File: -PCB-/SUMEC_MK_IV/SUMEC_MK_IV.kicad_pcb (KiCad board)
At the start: 2 copper layers, 82 parts, among them IC2 DRV8874PWPR, IC3 DRV8874PWPR, J2 TYPE-C-31-M-12, J3 Conn_01x06_Pin, J4 Conn_01x03_Pin, J5 Conn_01x06_Pin, J6 Conn_01x03_Pin, J7 Conn_01x06_Pin, J8 Conn_01x04_Pin, J9 Conn_01x03_Pin, SW1 SW_DPDT_x2, SW2 SW_Push, SW3 SW_Push, SW4 SW_Push, SW5 SW_Push, SW6 SW_Push, U1 TPS62133, U2 LM1084-3.3, U3 ESP32-S3-WROOM-1, U4 ESP32-S3-WROOM-1, U5 USBLC6-2SC6, U6 TSOP382xx

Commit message: Footprints added
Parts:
- removed C23, C24: 10uF.hb, Capacitor_Tantalum_SMD:CP_EIA-3216-18_Kemet-A_Pad1.58x1.35mm_HandSolder
- removed SW6: SW_Push, Button_Switch_SMD:SW_SPST_B3U-1000P
- removed U4: ESP32-S3-WROOM-1, PCM_Espressif:ESP32-S3-WROOM-1
- added C14: 100nF, Capacitor_SMD:C_0805_2012Metric_Pad1.18x1.45mm_HandSolder, F.Cu at (204.0, 91.0)
- added C17: 100nF.hb, Capacitor_SMD:C_0805_2012Metric_Pad1.18x1.45mm_HandSolder, F.Cu at (204.0, 100.1)
- added C18: 100nF.hb, Capacitor_SMD:C_0805_2012Metric_Pad1.18x1.45mm_HandSolder, F.Cu at (204.0, 103.1)
- added C19: 10uF.hb, Capacitor_Tantalum_SMD:CP_EIA-3216-18_Kemet-A_Pad1.58x1.35mm_HandSolder, F.Cu at (218.9, 101.7)
- added C20: 10uF.hb, Capacitor_Tantalum_SMD:CP_EIA-3216-18_Kemet-A_Pad1.58x1.35mm_HandSolder, F.Cu at (218.9, 104.8)
- added D1: D_Schottky, Diode_SMD:D_1206_3216Metric_Pad1.42x1.75mm_HandSolder, F.Cu at (170.0, 88.2)
- added D2: D_Schottky, Diode_SMD:D_1206_3216Metric_Pad1.42x1.75mm_HandSolder, F.Cu at (170.0, 91.6)
- added D6: LED, LED_SMD:LED_0805_2012Metric_Pad1.15x1.40mm_HandSolder, F.Cu at (102.7, 97.2)
- added D8: D_Schottky, Diode_SMD:D_1206_3216Metric_Pad1.42x1.75mm_HandSolder, F.Cu at (170.0, 95.0)
- added IC1: TPS565242DRLR, Package_TO_SOT_SMD:SOT-563, F.Cu at (184.5, 71.8)
- added J1: XT30PW-M, sumec_brd:XT30PW-M, F.Cu at (203.2, 69.8)
- added J10: Conn_01x04_Pin, Connector_Molex:Molex_PicoBlade_53398-0471_1x04-1MP_P1.25mm_Vertical, F.Cu at (125.3, 110.3)
- added J11: Conn_01x03_Pin, Connector_Molex:Molex_PicoBlade_53398-0371_1x03-1MP_P1.25mm_Vertical, F.Cu at (112.9, 124.2)
- added J12: TYPE-C-31-M-12, sumec-smdV2_library:USB_Type_C, F.Cu at (142.2, 40.5)
- added J13: Conn_01x06_Socket, Connector_JST:JST_SH_SM06B-SRSS-TB_1x06-1MP_P1.00mm_Horizontal, F.Cu at (126.8, 73.0)
- added J14: Conn_01x06_Socket, Connector_JST:JST_SH_SM06B-SRSS-TB_1x06-1MP_P1.00mm_Horizontal, F.Cu at (126.8, 80.6)
- added L1: 2.2uH, Inductor_SMD:L_Vishay_IHLP-1616, F.Cu at (172.8, 117.2)
- added L2: 1.5uH, Inductor_SMD:L_Vishay_IHLP-1212, F.Cu at (180.8, 71.8)
- added Q1: PMOS, Package_TO_SOT_SMD:SOT-23-3, F.Cu at (169.6, 99.1)
- added R20: 100R, Resistor_SMD:R_0805_2012Metric_Pad1.20x1.40mm_HandSolder, F.Cu at (102.6, 103.1)
- added R21: 100R, Resistor_SMD:R_0805_2012Metric_Pad1.20x1.40mm_HandSolder, F.Cu at (102.6, 106.1)
- added R22: 100R, Resistor_SMD:R_0805_2012Metric_Pad1.20x1.40mm_HandSolder, F.Cu at (102.6, 109.0)
- added R23: 0R, Resistor_SMD:R_0805_2012Metric_Pad1.20x1.40mm_HandSolder, F.Cu at (203.9, 119.9)
- added R24: 15R, Resistor_SMD:R_0805_2012Metric_Pad1.20x1.40mm_HandSolder, F.Cu at (203.9, 122.9)
- added R25: 15R, Resistor_SMD:R_0805_2012Metric_Pad1.20x1.40mm_HandSolder, F.Cu at (203.9, 125.8)
- added R5: 33k, Resistor_SMD:R_0805_2012Metric_Pad1.20x1.40mm_HandSolder, F.Cu at (138.7, 99.8)
- added R6: 10k, Resistor_SMD:R_0805_2012Metric_Pad1.20x1.40mm_HandSolder, F.Cu at (138.7, 102.8)
- C1: value 10uF.bck -> 22uF.vin; footprint Capacitor_Tantalum_SMD:CP_EIA-3216-18_Kemet-A_Pad1.58x1.35mm_HandSolder -> Capacitor_SMD:C_0805_2012Metric_Pad1.18x1.45mm_HandSolder
- C10: value 100nF -> 22uF; footprint Capacitor_SMD:C_0805_2012Metric -> Capacitor_Tantalum_SMD:CP_EIA-3528-21_Kemet-B_Pad1.50x2.35mm_HandSolder
- C11: value 10uF.reg -> 22uF; footprint Capacitor_Tantalum_SMD:CP_EIA-3216-18_Kemet-A_Pad1.58x1.35mm_HandSolder -> Capacitor_Tantalum_SMD:CP_EIA-3528-21_Kemet-B_Pad1.50x2.35mm_HandSolder
- C12: value 3.3nF -> 100nF.vout
- C13: value 10uF.reg -> 22nF; footprint Capacitor_Tantalum_SMD:CP_EIA-3216-18_Kemet-A_Pad1.58x1.35mm_HandSolder -> Capacitor_SMD:C_0805_2012Metric_Pad1.18x1.45mm_HandSolder
- C15: value 10uF.mcu -> 22nF; footprint Capacitor_Tantalum_SMD:CP_EIA-3216-18_Kemet-A_Pad1.58x1.35mm_HandSolder -> Capacitor_SMD:C_0805_2012Metric_Pad1.18x1.45mm_HandSolder
- C16: value 100nF.mcu -> 100nF
- C2: value 100nF.avin -> 100nF.vin
- C21, C22: value 100nF.hb -> 10uF.shrp; footprint Capacitor_SMD:C_0805_2012Metric_Pad1.18x1.45mm_HandSolder -> Capacitor_Tantalum_SMD:CP_EIA-3216-18_Kemet-A_Pad1.58x1.35mm_HandSolder
- C25: value 100nF.en -> 10uF.mcu; footprint Capacitor_SMD:C_0805_2012Metric_Pad1.18x1.45mm_HandSolder -> Capacitor_Tantalum_SMD:CP_EIA-3216-18_Kemet-A_Pad1.58x1.35mm_HandSolder
- C26: value 100nF.boot -> 100nF.mcu
- C28: value 10uF.shrp -> 100nF.en; footprint Capacitor_Tantalum_SMD:CP_EIA-3216-18_Kemet-A_Pad1.58x1.35mm_HandSolder -> Capacitor_SMD:C_0805_2012Metric_Pad1.18x1.45mm_HandSolder
- C29: value 10uF.shrp -> 100nF.boot; footprint Capacitor_Tantalum_SMD:CP_EIA-3216-18_Kemet-A_Pad1.58x1.35mm_HandSolder -> Capacitor_SMD:C_0805_2012Metric_Pad1.18x1.45mm_HandSolder
- C3: value 22uF -> 10uF.reg; footprint Capacitor_SMD:C_0805_2012Metric -> Capacitor_Tantalum_SMD:CP_EIA-3216-18_Kemet-A_Pad1.58x1.35mm_HandSolder
- C4: value 100nF -> 3.3nF; footprint Capacitor_SMD:C_0805_2012Metric -> Capacitor_SMD:C_0805_2012Metric_Pad1.18x1.45mm_HandSolder
- C5: value 10uF.mcu -> 10uF.pvin
- C6: value 100nF.mcu -> 10uF.reg; footprint Capacitor_SMD:C_0805_2012Metric_Pad1.18x1.45mm_HandSolder -> Capacitor_Tantalum_SMD:CP_EIA-3216-18_Kemet-A_Pad1.58x1.35mm_HandSolder
- C7: value 22uF -> 100nF.avin; footprint Capacitor_SMD:C_0805_2012Metric -> Capacitor_SMD:C_0805_2012Metric_Pad1.18x1.45mm_HandSolder
- C8, C9: footprint Capacitor_SMD:C_0805_2012Metric -> Capacitor_Tantalum_SMD:CP_EIA-3528-21_Kemet-B_Pad1.50x2.35mm_HandSolder
- D7: value LED -> D_Schottky; footprint LED_SMD:LED_0805_2012Metric_Pad1.15x1.40mm_HandSolder -> Diode_SMD:D_1206_3216Metric_Pad1.42x1.75mm_HandSolder
- J2: value TYPE-C-31-M-12 -> Conn_01x03_Pin; footprint sumec-smdV2_library:USB_Type_C -> Connector_Molex:Molex_PicoBlade_53398-0371_1x03-1MP_P1.25mm_Vertical
- J4, J6: value Conn_01x03_Pin -> Conn_01x06_Pin; footprint Connector_Molex:Molex_PicoBlade_53398-0371_1x03-1MP_P1.25mm_Vertical -> Connector_Molex:Molex_PicoBlade_53398-0671_1x06-1MP_P1.25mm_Vertical
- J5, J7: value Conn_01x06_Pin -> Conn_01x03_Pin; footprint Connector_Molex:Molex_PicoBlade_53398-0671_1x06-1MP_P1.25mm_Vertical -> Connector_Molex:Molex_PicoBlade_53398-0371_1x03-1MP_P1.25mm_Vertical
- J8: value Conn_01x04_Pin -> Conn_01x03_Pin; footprint Connector_Molex:Molex_PicoBlade_53398-0471_1x04-1MP_P1.25mm_Vertical -> Connector_Molex:Molex_PicoBlade_53398-0371_1x03-1MP_P1.25mm_Vertical
- R1: value 100k -> 20k; footprint Resistor_SMD:R_0805_2012Metric -> Resistor_SMD:R_0805_2012Metric_Pad1.20x1.40mm_HandSolder
- R10: value 10k.mcu -> 0R/R-Imode
- R11: value 0R -> 10k; footprint Resistor_SMD:R_1206_3216Metric_Pad1.30x1.75mm_HandSolder -> Resistor_SMD:R_0805_2012Metric_Pad1.20x1.40mm_HandSolder
- R12: value 15R -> 10k
- R13: value 15R -> 0R
- R14: value 10k -> 0R
- R15: value 100 -> 0R
- R16: value R -> 0R; footprint sumec-remote_library:purosidenegative -> Resistor_SMD:R_0805_2012Metric_Pad1.20x1.40mm_HandSolder
- R17: value R -> 10k; footprint sumec-smdV2_library:SPS LOGO -> Resistor_SMD:R_0805_2012Metric_Pad1.20x1.40mm_HandSolder
- R18: value R -> 100; footprint sumec-remote_library:boi -> Resistor_SMD:R_0805_2012Metric_Pad1.20x1.40mm_HandSolder
- R19: value R -> 560R; footprint sumec-smdV2_library:Logo -> Resistor_SMD:R_0805_2012Metric_Pad1.20x1.40mm_HandSolder
- R2: value 22k -> 30k; footprint Resistor_SMD:R_0805_2012Metric -> Resistor_SMD:R_0805_2012Metric_Pad1.20x1.40mm_HandSolder
- R26: value 0R -> 10k.mcu; footprint Resistor_SMD:R_1206_3216Metric_Pad1.30x1.75mm_HandSolder -> Resistor_SMD:R_0805_2012Metric_Pad1.20x1.40mm_HandSolder
- R27: value 0R -> R; footprint Resistor_SMD:R_1206_3216Metric_Pad1.30x1.75mm_HandSolder -> sumec-remote_library:purosidenegative
- R28: value 0R -> R; footprint Resistor_SMD:R_1206_3216Metric_Pad1.30x1.75mm_HandSolder -> sumec-smdV2_library:SPS LOGO
- R29: value 0R -> R; footprint Resistor_SMD:R_1206_3216Metric_Pad1.30x1.75mm_HandSolder -> sumec-remote_library:boi
- R3: value 150k -> 100k; footprint Resistor_SMD:R_0805_2012Metric -> Resistor_SMD:R_0805_2012Metric_Pad1.20x1.40mm_HandSolder
- R30: value 100R -> R; footprint Resistor_SMD:R_0805_2012Metric_Pad1.20x1.40mm_HandSolder -> sumec-smdV2_library:Logo
- R4: value 33k -> 150k; footprint Resistor_SMD:R_0805_2012Metric -> Resistor_SMD:R_0805_2012Metric_Pad1.20x1.40mm_HandSolder
- R7: value 100R -> 0R/R-Ipropi
- R8: value 100R -> 0R/R-Imode
- R9: value 560R -> 0R/R-Ipropi
- SW1: footprint sumec-smdV2_library:Custom_SPDT_4.8mm_Switch -> sumec_brd:Custom_SPDT_4.7mm_Switch
- SW2, SW3, SW4, SW5: footprint Button_Switch_SMD:SW_SPST_B3U-1000P -> Button_Switch_SMD:SW_SPST_EVQPE1
- TP1: footprint TestPoint:TestPoint_Loop_D1.80mm_Drill1.0mm_Beaded -> TestPoint:TestPoint_Pad_D1.0mm
- TP2: footprint TestPoint:TestPoint_Pad_D1.5mm -> TestPoint:TestPoint_Loop_D1.80mm_Drill1.0mm_Beaded
- TP4: footprint TestPoint:TestPoint_Pad_D1.5mm -> TestPoint:TestPoint_Pad_1.0x1.0mm
- U1: value TPS62133 -> LM1084-3.3; footprint Package_DFN_QFN:VQFN-16-1EP_3x3mm_P0.5mm_EP1.68x1.68mm_ThermalVias -> Package_TO_SOT_SMD:TO-263-3_TabPin2
- U2: value LM1084-3.3 -> TPS62133; footprint Package_TO_SOT_SMD:TO-263-3_TabPin2 -> Package_DFN_QFN:VQFN-16-1EP_3x3mm_P0.5mm_EP1.68x1.68mm_ThermalVias
- U3: value ESP32-S3-WROOM-1 -> TSOP382xx; footprint RF_Module:ESP32-S3-WROOM-1 -> sumec-smdV2_library:TSOP
- U5: value USBLC6-2SC6 -> ESP32-S3-WROOM-1; footprint Package_TO_SOT_SMD:TSOT-23-6_HandSoldering -> RF_Module:ESP32-S3-WROOM-1
- U6: value TSOP382xx -> USBLC6-2SC6; footprint sumec-smdV2_library:TSOP -> Package_TO_SOT_SMD:TSOT-23-6_HandSoldering
- moved R16 151.2 mm to (213.5, 96.8)
- moved TP5 141.9 mm to (259.5, 67.2)
- moved TP6 141.4 mm to (259.5, 72.1)
- moved R27 138.5 mm to (74.6, 58.5)
- moved TP1 136.9 mm to (245.2, 61.8)
- moved U5 135.4 mm to (75.7, 114.8)
- moved R28 135.0 mm to (201.9, -20.3)
- moved R17 130.3 mm to (131.8, 115.8)
- moved TP4 126.8 mm to (242.2, 61.8)
- moved H1 125.2 mm to (240.8, 102.5)
- moved H2 125.2 mm to (240.8, 110.5)
- moved H3 125.2 mm to (240.8, 118.4)
- moved H4 125.2 mm to (240.8, 126.3)
- moved TP3 122.3 mm to (239.0, 61.8)
- moved R8 122.2 mm to (208.8, 91.0)
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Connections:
- C1 pad 1: +12V -> Net-(IC1-VIN)
- C1 pad 2: GND -> +5V
- C10 pad 1: VCC -> +3V3
- C11 pad 1: +5V -> +3V3
- C12 pad 1: GND -> +3V3
- C12 pad 2: Net-(U1-SS/TR) -> GND
- C13 pad 1: +3V3 -> Net-(IC2-CPL)
- C13 pad 2: GND -> Net-(IC2-CPH)
- C15 pad 1: +3V3 -> Net-(IC3-CPL)
- C15 pad 2: GND -> Net-(IC3-CPH)
- C16 pad 1: +3V3 -> Net-(IC3-VCP)
- C16 pad 2: GND -> +12V
- C2 pad 1: +12V -> Net-(IC1-VIN)
- C2 pad 2: GND -> +5V
- C21 pad 1: GND -> +3V3
- C21 pad 2: +12V -> GND
- C22 pad 1: GND -> +3V3
- C22 pad 2: +12V -> GND
- C25 pad 1: EN -> +3V3
- C26 pad 1: BOOT -> +3V3
- C28 pad 1: +3V3 -> EN
- C29 pad 1: +3V3 -> BOOT
- C4 pad 1: +5V -> GND
- C4 pad 2: GND -> Net-(U2-SS/TR)
- C5 pad 1: +3V3 -> +12V
- C7 pad 1: VCC -> +12V
- C8 pad 1: VCC -> VOUT 5V
- C9 pad 1: VCC -> +3V3
- D3 pad 2: LED1 -> +12V
- D5 pad 2: +12V -> LED2
- D7 pad 1: Net-(D7-K) -> VBUS 5V
- D7 pad 2: LED2 -> Net-(D7-A)
- J4 pad 1: SHARP 1 -> +5V
- J4 pad 2: +3V3 -> SDA
- J4 pad 3: GND -> SCL
- J5 pad 1: +5V -> SHARP 2
- J5 pad 2: SDA -> +3V3
- J5 pad 3: SCL -> GND
- J6 pad 1: SHARP 2 -> +5V
- J6 pad 2: +3V3 -> SDA
- J6 pad 3: GND -> SCL
- J7 pad 1: +5V -> POL 3
- J7 pad 2: SDA -> +3V3
- J7 pad 3: SCL -> GND
- J8 pad 1: QRE1113 A -> POL 1
- J8 pad 2: GND -> +3V3
- J8 pad 3: +3V3 -> GND
- J9 pad 1: QRE1113 C -> POL 2
- J9 pad 2: Net-(J9-Pin_2) -> +3V3
- R1 pad 1: +5V -> Net-(D8-K)
- R1 pad 2: /POWER_SUPPLY/En_3V3 -> +5V
- R10 pad 1: EN -> GND
- R10 pad 2: +3V3 -> Net-(IC3-IMODE)
- R11 pad 1: Net-(J2-SHIELD-PadS1) -> +3V3
- R11 pad 2: GND -> nFAULT
- R12 pad 1: D+ IN -> +3V3
- R12 pad 2: Net-(R12-Pad2) -> nFAULT
- R13 pad 1: D- IN -> GND
- R13 pad 2: Net-(R13-Pad2) -> Net-(IC2-PMODE)
- R14 pad 2: QRE1113 C -> Net-(IC2-PMODE)
- R15 pad 1: +3V3 -> GND
- R15 pad 2: Net-(J9-Pin_2) -> Net-(IC3-PMODE)
- R2 pad 1: /POWER_SUPPLY/En_3V3 -> Net-(D8-K)
- R26 pad 1: GND -> EN
- R26 pad 2: Net-(IC2-PMODE) -> +3V3
- R3 pad 1: VCC -> VOUT 5V
- R3 pad 2: Net-(IC1-FB) -> Net-(U2-PG)
- R4 pad 1: Net-(IC1-FB) -> +3V3
- R4 pad 2: GND -> FB
- R7 pad 1: Net-(D3-K) -> GND
- R7 pad 2: GND -> IPROPI_ADC
- R8 pad 1: Net-(D4-K) -> GND
- R8 pad 2: GND -> Net-(IC2-IMODE)
- R9 pad 1: Net-(D5-K) -> GND
- R9 pad 2: GND -> IPROPI_ADC
- SW4 pad 2: TEST PROGRAM -> TEST PROGRAM 1
- SW5 pad 2: unconnected-(SW5-Pad2) -> TEST PROGRAM 2
- TP1 pad 1: +3V3 -> +5V
- TP2 pad 1: SCL -> +3V3
- TP3 pad 1: SDA -> unconnected-(TP3-Pad1)
- TP4 pad 1: D- -> unconnected-(TP4-Pad1)
- TP5 pad 1: +5V -> D-
- U1 pad 1: Net-(L2-Pad1) -> GND
- U1 pad 2: Net-(L2-Pad1) -> +3V3
- U1 pad 3: Net-(L2-Pad1) -> +5V
- U2 pad 1: GND -> Net-(L1-Pad1)
- U2 pad 2: +3V3 -> Net-(L1-Pad1)
- U2 pad 3: +5V -> Net-(L1-Pad1)
- U3 pad 1: Net-(U3-GND-Pad1) -> IR MODULE
- U3 pad 2: +3V3 -> GND
- U3 pad 3: EN -> +3V3
- U5 pad 1: Net-(R12-Pad2) -> Net-(U5-GND-Pad1)
- U5 pad 2: GND -> +3V3
- U5 pad 3: Net-(R13-Pad2) -> EN
- U5 pad 4: D- -> QRE1113 B
- U5 pad 5: VBUS 5V -> QRE1113 A
- U5 pad 6: D+ -> QRE1113 C
- U6 pad 1: IR MODULE -> Net-(R24-Pad2)
- U6 pad 3: +3V3 -> Net-(R25-Pad2)

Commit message: MK_IV PCB update
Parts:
- removed C28: 100nF.en, Capacitor_SMD:C_0805_2012Metric_Pad1.18x1.45mm_HandSolder
- removed C29: 100nF.boot, Capacitor_SMD:C_0805_2012Metric_Pad1.18x1.45mm_HandSolder
- removed U6: USBLC6-2SC6, Package_TO_SOT_SMD:TSOT-23-6_HandSoldering
- added C23: 10uF.mcu, Capacitor_Tantalum_SMD:CP_EIA-3216-18_Kemet-A_Pad1.58x1.35mm_HandSolder, B.Cu at (183.5, 118.0)
- added C24: 100nF.mcu, Capacitor_SMD:C_0805_2012Metric_Pad1.18x1.45mm_HandSolder, B.Cu at (181.2, 117.5)
- added U4: ESP32-S3-WROOM-1, RF_Module:ESP32-S3-WROOM-1, F.Cu at (190.0, 120.5)
- C1: value 22uF.vin -> 10uF.reg; footprint Capacitor_SMD:C_0805_2012Metric_Pad1.18x1.45mm_HandSolder -> Capacitor_Tantalum_SMD:CP_EIA-3216-18_Kemet-A_Pad1.58x1.35mm_HandSolder
- C10, C11, C12, C5, C9, D1, D2, IC1, Q1, R23, R26, R4, R5, U2: moved to B.Cu
- C2: value 100nF.vin -> 10uF.reg; footprint Capacitor_SMD:C_0805_2012Metric_Pad1.18x1.45mm_HandSolder -> Capacitor_Tantalum_SMD:CP_EIA-3216-18_Kemet-A_Pad1.58x1.35mm_HandSolder
- C25: value 10uF.mcu -> 100nF; footprint Capacitor_Tantalum_SMD:CP_EIA-3216-18_Kemet-A_Pad1.58x1.35mm_HandSolder -> Capacitor_SMD:C_0805_2012Metric_Pad1.18x1.45mm_HandSolder
- C26: value 100nF.mcu -> 100nF.en; moved to B.Cu
- C27: value 100nF -> 100nF.boot; moved to B.Cu
- C3: value 10uF.reg -> 3.3nF; footprint Capacitor_Tantalum_SMD:CP_EIA-3216-18_Kemet-A_Pad1.58x1.35mm_HandSolder -> Capacitor_SMD:C_0805_2012Metric_Pad1.18x1.45mm_HandSolder; moved to B.Cu
- C4: value 3.3nF -> 22uF; footprint Capacitor_SMD:C_0805_2012Metric_Pad1.18x1.45mm_HandSolder -> Capacitor_Tantalum_SMD:CP_EIA-3528-21_Kemet-B_Pad1.50x2.35mm_HandSolder; moved to B.Cu
- C6: value 10uF.reg -> 100nF.vin; footprint Capacitor_Tantalum_SMD:CP_EIA-3216-18_Kemet-A_Pad1.58x1.35mm_HandSolder -> Capacitor_SMD:C_0805_2012Metric_Pad1.18x1.45mm_HandSolder; moved to B.Cu
- C7: value 100nF.avin -> 22uF; footprint Capacitor_SMD:C_0805_2012Metric_Pad1.18x1.45mm_HandSolder -> Capacitor_Tantalum_SMD:CP_EIA-3528-21_Kemet-B_Pad1.50x2.35mm_HandSolder; moved to B.Cu
- C8: value 22uF -> 100nF.avin; footprint Capacitor_Tantalum_SMD:CP_EIA-3528-21_Kemet-B_Pad1.50x2.35mm_HandSolder -> Capacitor_SMD:C_0805_2012Metric_Pad1.18x1.45mm_HandSolder; moved to B.Cu
- D3: value LED -> D_Schottky; footprint LED_SMD:LED_0805_2012Metric_Pad1.15x1.40mm_HandSolder -> Diode_SMD:D_1206_3216Metric_Pad1.42x1.75mm_HandSolder; moved to B.Cu
- D7: value D_Schottky -> LED; footprint Diode_SMD:D_1206_3216Metric_Pad1.42x1.75mm_HandSolder -> LED_SMD:LED_0805_2012Metric_Pad1.15x1.40mm_HandSolder
- L1: value 2.2uH -> 1.5uH; footprint Inductor_SMD:L_Vishay_IHLP-1616 -> Inductor_SMD:L_Vishay_IHLP-1212; moved to B.Cu
- L2: value 1.5uH -> 2.2uH; footprint Inductor_SMD:L_Vishay_IHLP-1212 -> Inductor_SMD:L_Vishay_IHLP-1616; moved to B.Cu
- R1: value 20k -> 10k; moved to B.Cu
- R2: value 30k -> 20k; moved to B.Cu
- R3: value 100k -> 30k; moved to B.Cu
- R6: value 10k -> 100k; moved to B.Cu
- TP3: footprint TestPoint:TestPoint_Pad_D1.5mm -> TestPoint:TestPoint_Pad_1.0x1.0mm
- TP4: footprint TestPoint:TestPoint_Pad_1.0x1.0mm -> TestPoint:TestPoint_Pad_D1.5mm
- U5: value ESP32-S3-WROOM-1 -> USBLC6-2SC6; footprint RF_Module:ESP32-S3-WROOM-1 -> Package_TO_SOT_SMD:TSOT-23-6_HandSoldering
- moved R27 156.4 mm to (-68.2, -5.34)
- moved R28 156.4 mm to (59.1, -84.1)
- moved R29 156.4 mm to (-35.5, -10.2)
- moved R30 156.4 mm to (-23.6, -25.9)
- moved TP5 153.4 mm to (154.2, 178.8)
- moved TP6 152.4 mm to (154.2, 182.3)
- moved C26 146.2 mm to (205.2, 116.8)
- moved TP4 143.6 mm to (154.2, 175.2)
- moved TP1 143.2 mm to (157.5, 174.9)
- moved TP3 142.0 mm to (157.5, 178.0)
- moved TP2 133.3 mm to (166.2, 175.8)
- moved C2 129.0 mm to (278.0, 29.5), turned to 90 degrees
- moved C1 125.3 mm to (275.5, 29.5), turned to 90 degrees
- moved U1 120.1 mm to (278.0, 42.4), turned to -90 degrees
- moved D4 113.8 mm to (206.2, 138.2), turned to 90 degrees
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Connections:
- C1 pad 1: Net-(IC1-VIN) -> +5V
- C1 pad 2: +5V -> GND
- C10 pad 2: GND -> Net-(C10-Pad2)
- C11 pad 1: +3V3 -> VOUT 5V
- C12 pad 2: GND -> Net-(C10-Pad2)
- C2 pad 1: Net-(IC1-VIN) -> +3V3
- C2 pad 2: +5V -> GND
- C25 pad 1: +3V3 -> VBUS 5V
- C26 pad 1: +3V3 -> EN
- C27 pad 1: VBUS 5V -> BOOT
- C3 pad 1: +5V -> GND
- C3 pad 2: GND -> Net-(U2-SS/TR)
- C4 pad 1: GND -> +5V
- C4 pad 2: Net-(U2-SS/TR) -> GND
- C6 pad 1: +3V3 -> +5V
- C7 pad 1: +12V -> +3V3
- C7 pad 2: GND -> Net-(C10-Pad2)
- C8 pad 1: VOUT 5V -> +12V
- C9 pad 2: GND -> Net-(C10-Pad2)
- D3 pad 2: +12V -> GND
- D4 pad 2: LED2 -> +12V
- D5 pad 2: LED2 -> LED1
- D6 pad 2: LED1 -> LED2
- D7 pad 1: VBUS 5V -> Net-(D7-K)
- D7 pad 2: Net-(D7-A) -> LED3
- D8 pad 1: Net-(D8-K) -> VBUS 5V
- D8 pad 2: GND -> Net-(D8-A)
- IC1 pad 1: Net-(IC1-VIN) -> +5V
- IC1 pad 5: Net-(D8-K) -> Net-(D3-K)
- J12 pad A4_B9: Net-(D7-A) -> Net-(D8-A)
- J12 pad B4_A9: Net-(D7-A) -> Net-(D8-A)
- L1 pad 1: Net-(L1-Pad1) -> Net-(IC1-SW)
- L1 pad 2: VOUT 5V -> +3V3
- L2 pad 1: Net-(IC1-SW) -> Net-(L2-Pad1)
- L2 pad 2: +3V3 -> VOUT 5V
- R1 pad 1: Net-(D8-K) -> VBUS 5V
- R1 pad 2: +5V -> GND
- R19 pad 1: Net-(D3-K) -> Net-(D4-K)
- R2 pad 1: Net-(D8-K) -> Net-(D3-K)
- R2 pad 2: GND -> +5V
- R20 pad 1: Net-(D4-K) -> Net-(D5-K)
- R21 pad 1: Net-(D5-K) -> Net-(D6-K)
- R22 pad 1: Net-(D6-K) -> Net-(D7-K)
- R3 pad 1: VOUT 5V -> Net-(D3-K)
- R3 pad 2: Net-(U2-PG) -> GND
- R6 pad 1: VBUS 5V -> VOUT 5V
- R6 pad 2: GND -> Net-(U2-PG)
- U2 pad 1: Net-(L1-Pad1) -> Net-(L2-Pad1)
- U2 pad 2: Net-(L1-Pad1) -> Net-(L2-Pad1)
- U2 pad 3: Net-(L1-Pad1) -> Net-(L2-Pad1)
- U5 pad 1: Net-(U5-GND-Pad1) -> Net-(R24-Pad2)
- U5 pad 2: +3V3 -> GND
- U5 pad 3: EN -> Net-(R25-Pad2)
- U5 pad 4: QRE1113 B -> D-
- U5 pad 5: QRE1113 A -> VBUS 5V
- U5 pad 6: QRE1113 C -> D+
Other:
- board outline added: 80 x 45 mm
- copper layers 2 -> 4

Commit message: MK_IV layout update
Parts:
- removed TP6: TestPoint, TestPoint:TestPoint_Pad_D1.5mm
- C14, C16, C19, C20, C21, C22, J10, J11, J13, J14, J2, J5, J7, J8, J9, R11, R12, R14, R16, R17, R18: moved to B.Cu
- TP1: footprint TestPoint:TestPoint_Pad_D1.0mm -> TestPoint:TestPoint_Pad_1.0x1.0mm
- TP2: footprint TestPoint:TestPoint_Loop_D1.80mm_Drill1.0mm_Beaded -> TestPoint:TestPoint_Pad_1.0x1.0mm
- TP4, TP5: footprint TestPoint:TestPoint_Pad_D1.5mm -> TestPoint:TestPoint_Pad_1.0x1.0mm
- moved J2 118.5 mm to (219.4, 136.2), turned to -90 degrees
- moved J7 111.9 mm to (213.0, 154.7), turned to 180 degrees
- moved J11 106.6 mm to (190.0, 117.3)
- moved J9 101.7 mm to (201.8, 154.7), turned to 180 degrees
- moved C19 100.8 mm to (188.0, 143.2), turned to 90 degrees
- moved IC2 100.1 mm to (193.0, 146.2), turned to 180 degrees
- moved J3 97.4 mm to (211.0, 155.8), turned to 180 degrees
- moved IC3 97.0 mm to (207.8, 146.2), turned to 180 degrees
- moved C20 95.5 mm to (202.8, 143.2), turned to 90 degrees
- moved R13 95.3 mm to (191.0, 150.0), turned to 180 degrees
- moved R15 94.2 mm to (205.8, 150.0), turned to 180 degrees
- moved R14 93.6 mm to (191.0, 150.0), turned to 180 degrees
- moved R16 91.9 mm to (205.8, 150.0), turned to 180 degrees
- moved J13 90.2 mm to (195.1, 134.1)
- moved C13 88.8 mm to (188.0, 147.8), turned to 90 degrees
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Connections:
- TP3 pad 1: unconnected-(TP3-Pad1) -> IR MODULE
- TP4 pad 1: unconnected-(TP4-Pad1) -> OUT 1A
- TP5 pad 1: D- -> OUT 1B

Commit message: PCB routing
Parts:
- U3: footprint sumec-smdV2_library:TSOP -> sumec_brd:TSOP
- moved J14 2.43 mm to (183.5, 132.2), turned to -90 degrees
- moved J13 2.37 mm to (196.5, 132.2), turned to 90 degrees
- moved J10 1.05 mm to (190.0, 155.8), turned to 0 degrees
- moved J7 1.05 mm to (213.0, 155.8), turned to 0 degrees
- moved J8 1.05 mm to (178.5, 155.8), turned to 0 degrees
- moved J9 1.05 mm to (201.8, 155.8), turned to 0 degrees
- moved C25 0.96 mm to (167.0, 124.8)
- turned D1 to 0 degrees
- turned D2 to 0 degrees
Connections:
- J13 pad 1: M1A -> GND
- J13 pad 2: M1B -> OUT 1B
- J13 pad 3: +3V3 -> OUT 1A
- J13 pad 4: OUT 1A -> +3V3
- J13 pad 5: OUT 1B -> M1B
- J13 pad 6: GND -> M1A
- J14 pad 1: M2A -> GND
- J14 pad 2: M2B -> OUT 2B
- J14 pad 3: +3V3 -> OUT 2A
- J14 pad 4: OUT 2A -> +3V3
- J14 pad 5: OUT 2B -> M2B
- J14 pad 6: GND -> M2A
- TP3 pad 1: IR MODULE -> OUT 1A
- TP4 pad 1: OUT 1A -> OUT 1B
- TP5 pad 1: OUT 1B -> IR MODULE
- U4 pad 12: OUT 1B -> unconnected-(U4-IO8-Pad12)
- U4 pad 21: unconnected-(U4-IO13-Pad21) -> QRE1113 A
- U4 pad 22: POL 1 -> QRE1113 B
- U4 pad 24: TEST PROGRAM 1 -> unconnected-(U4-IO47-Pad24)
- U4 pad 25: TEST PROGRAM 2 -> unconnected-(U4-IO48-Pad25)
- U4 pad 28: PWM1 -> OUT 1B
- U4 pad 29: PWM2 -> OUT 1A
- U4 pad 30: IN1 -> PWM1
- U4 pad 31: IN2 -> PWM2
- U4 pad 32: nSLEEP -> IN1
- U4 pad 33: nFAULT -> IN2
- U4 pad 34: SHARP 2 -> nSLEEP
- U4 pad 35: SHARP 1 -> nFAULT
- U4 pad 38: POL 3 -> TEST PROGRAM 1
- U4 pad 39: IPROPI_ADC -> TEST PROGRAM 2
- U4 pad 4: QRE1113 B -> unconnected-(U4-IO4-Pad4)
- U4 pad 5: QRE1113 A -> unconnected-(U4-IO5-Pad5)
- U4 pad 6: QRE1113 C -> SHARP 2
- U4 pad 7: OUT 1A -> unconnected-(U4-IO7-Pad7)
- U4 pad 8: OUT 2A -> unconnected-(U4-IO15-Pad8)
- U4 pad 9: OUT 2B -> unconnected-(U4-IO16-Pad9)
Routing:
- net VOUT 5V: track 0.00 -> 28.5 mm, vias 0 -> 3
- net +12V: track 0.00 -> 28.4 mm, vias 0 -> 3
- net +3V3: track 0.00 -> 19.8 mm
- net Net-(J12-SHIELD-PadS1): track 0.00 -> 18.7 mm
- net Net-(C10-Pad2): track 0.00 -> 16.3 mm
- net VBUS 5V: track 0.00 -> 14.8 mm, vias 0 -> 2
- net +5V: track 0.00 -> 10.9 mm, vias 0 -> 2
- net Net-(D8-A): track 0.00 -> 9.56 mm
- net Net-(D3-K): track 0.00 -> 8.00 mm
- net VBATT: track 0.00 -> 7.27 mm
- net Net-(L2-Pad1): track 0.00 -> 5.40 mm
- net GND: track 0.00 -> 3.24 mm
- net Net-(U2-PG): track 0.00 -> 3.17 mm
- net Net-(U2-SS/TR): track 0.00 -> 2.51 mm
- net Net-(R25-Pad2): track 0.00 -> 2.31 mm
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- added copper zone on In2.Cu, net +12V
- added copper zone on In1.Cu, net +3V3
- added copper zone on In2.Cu, net +5V
- added copper zone on B.Cu, net GND
- added copper zone on F.Cu, net GND
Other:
- board text added: "check connecotors check pours"

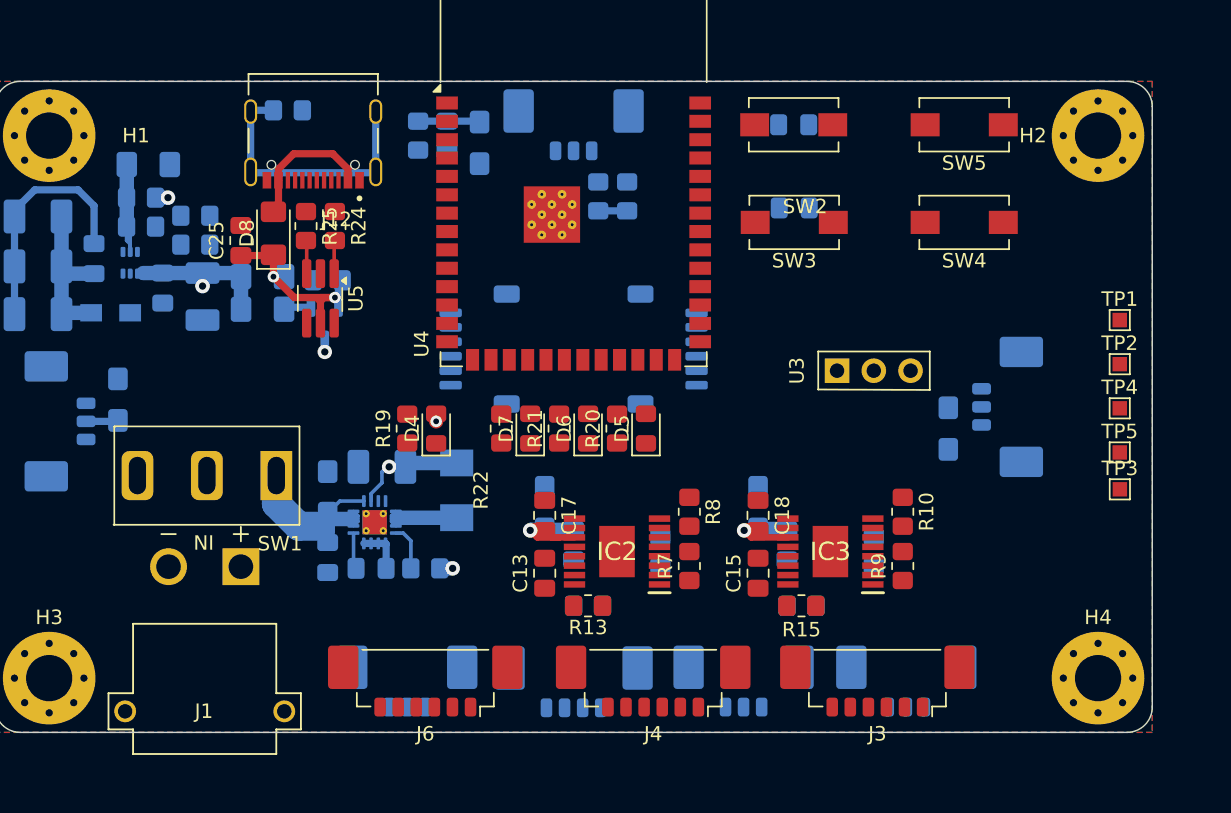
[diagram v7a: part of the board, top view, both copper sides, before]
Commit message: Small PCB routing
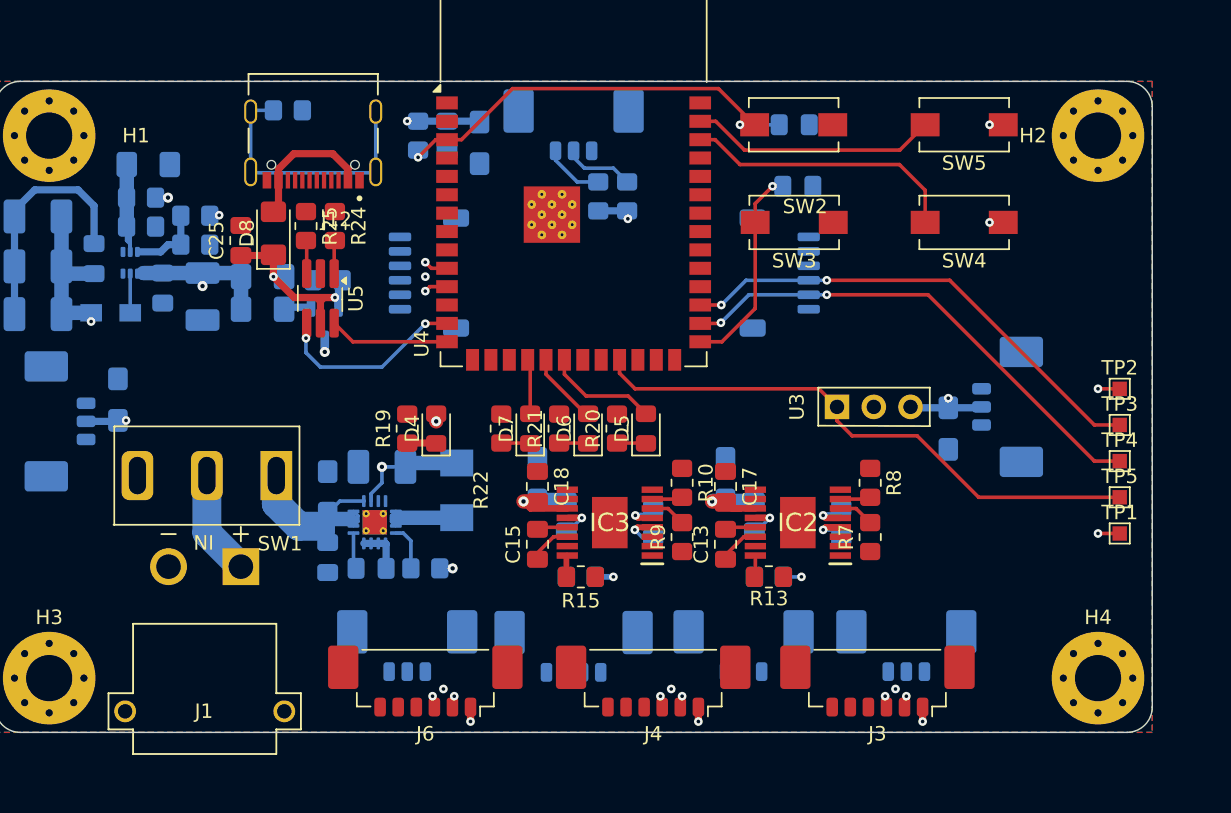
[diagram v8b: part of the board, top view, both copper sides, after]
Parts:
- moved C15 15.4 mm to (187.5, 145.8)
- moved C16 15.4 mm to (189.5, 143.8)
- moved C18 15.4 mm to (187.5, 141.8)
- moved C20 15.4 mm to (187.5, 141.2)
- moved IC3 15.4 mm to (192.5, 144.2)
- moved R10 15.4 mm to (197.5, 141.5)
- moved R12 15.4 mm to (195.5, 144.2)
- moved R15 15.4 mm to (190.5, 148.0)
- moved R16 15.4 mm to (190.5, 148.0)
- moved R9 15.4 mm to (197.5, 145.2)
- moved TP1 14.8 mm to (227.8, 145.0)
- moved C13 12.7 mm to (200.5, 145.8)
- moved C14 12.7 mm to (202.5, 143.8)
- moved C17 12.7 mm to (200.5, 141.8)
- moved C19 12.7 mm to (200.5, 141.2)
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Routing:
- net SCL: track 0.00 -> 68.1 mm, vias 0 -> 4
- net SDA: track 0.00 -> 67.5 mm, vias 0 -> 4
- net IR MODULE: track 0.00 -> 39.6 mm
- net OUT 1B: track 0.00 -> 34.6 mm, vias 0 -> 2
- net OUT 1A: track 0.00 -> 33.9 mm, vias 0 -> 2
- net EN: track 0.00 -> 29.0 mm, vias 0 -> 2
- net +3V3: track 19.8 -> 39.9 mm, vias 0 -> 13
- net TEST PROGRAM 1: track 0.00 -> 19.2 mm
- net TEST PROGRAM 2: track 0.00 -> 17.1 mm
- net BOOT: track 0.00 -> 14.4 mm, vias 0 -> 1
- net D-: track 0.00 -> 13.5 mm, vias 0 -> 2
- net D+: track 0.00 -> 8.33 mm
- net LED1: track 0.00 -> 7.76 mm
- net nFAULT: track 0.00 -> 5.73 mm, vias 0 -> 2
- net FB: track 0.00 -> 5.09 mm
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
